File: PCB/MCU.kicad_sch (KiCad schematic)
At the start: 17 parts, among them J2 Conn_01x05_Pin, SW1 SW_Push, U1 STM32WLE5CCUx

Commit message: added power block, pheripherial
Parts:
- SW1: value SW_Push -> SKRKAHE020
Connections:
- net UART_RX renamed UART0_RX
- net UART_TX renamed UART0_TX
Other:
- added sheet Pheripherials (pheripherials.kicad_sch)
- moved on the sheet: C1, J2, R1, R2, R3, SW1

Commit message: added GPS, charging IC, SHT41, and started working on the RF
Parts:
- added C16: 100nF, 1_capacitor_SMD:C_0402_1005Metric, symbol 0_generic_component:C
- added C17: 47pF, 1_capacitor_SMD:C_0402_1005Metric, symbol 0_generic_component:C
- added C18: 1,2pF, 1_capacitor_SMD:C_0402_1005Metric, symbol 0_generic_component:C
- added C19: 220nF, 1_capacitor_SMD:C_0402_1005Metric, symbol 0_generic_component:C
- added C20: 10pF, 1_capacitor_SMD:C_0402_1005Metric, symbol 0_generic_component:C
- added FB1: 1400Ω/1GHz, 2_inductor_SMD:L_0402_1005Metric, symbol 0_generic_component:ferrite_bead
- added J3: Conn_01x02_Pin, 300_pin_header_connector:PinHeader_1x02_P2.54mm_Vertical, symbol 0_generic_component:Conn_01x02_Pin
- added R12: 220Ω, 0_resistor_SMD:R_0402_1005Metric, symbol 0_generic_component:R
- added R13: 10KΩ, 0_resistor_SMD:R_0402_1005Metric, symbol 0_generic_component:R
- added Y1: ECS-TXO-25CSMV, 20_oscillator:ECS-TXO-25CSMV, symbol 20_oscillator:ECS-TXO-25CSMV
- U1: Current ~3.5mA in RUN, 120mA 868 Tx -> ~5mA in RX, 120mA 868 Tx
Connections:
- net GND: no longer C1.2, C10.2, C11.2, C12.2, C13.2, C2.2, C6.2, C7.2, C8.2, C9.2, R2.2, SW1.1, U1.48 (VSSSMPS), U1.49 (VSS)
- net UART1_RX: now also U1.10 (PA3)
- net UART1_TX: now also U1.9 (PA2)
- net PH3-BOOT0: now reaches U1.19 (PH3)
- net PH3-BOOT0: now also J3.2 (Pin_2), R13.1
- net RFI_P: now reaches U1.20 (RFI_P)
- net RFI_N: now reaches U1.21 (RFI_N)
- net RFO_HP: now reaches U1.23 (RFO_HP)
- net VR_PA: now reaches U1.24 (VR_PA)
- net OSC_IN: now reaches U1.26 (OSC_IN)
- net OSC_IN: now also C20.2
- net PB0_VDD_TCXO: now reaches U1.30 (PB0)
- net PB0_VDD_TCXO: now also C16.1, C17.1, C18.1, FB1.1
- new net: C20.1, R12.2
- new net: C19.2, FB1.2, Y1.4 (VDD)
- new net: R12.1, Y1.3 (OUTPUT)
- new net +3.3V: J3.1 (Pin_1)
- new net GNDREF: C1.2, C10.2, C11.2, C12.2, C13.2, C16.2, C17.2, C18.2, C19.1, C2.2, C6.2, C7.2, C8.2, C9.2, R13.2, R2.2, SW1.1, U1.48 (VSSSMPS), U1.49 (VSS), Y1.1 (GND), Y1.2 (GND)
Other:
- added sheet RF Frontend (RFfrontend.kicad_sch)
- note added: "Pin defines are based on the wio E5 and rak3172 MT definition."
- moved on the sheet: C1, J2, R1, R2, R3, SW1

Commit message: ported the main mcu from the inpiration board
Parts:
- added C21, C22, C23, C25: 33pF, 1_capacitor_SMD:C_0402_1005Metric, symbol 0_generic_component:C
- added C24, C26: 4,7uF, 1_capacitor_SMD:C_1206_3216Metric, symbol 0_generic_component:C
- added C27, C29, C30, C33: 100nF, 1_capacitor_SMD:C_0402_1005Metric, symbol 0_generic_component:C
- added C28: 470nF, 1_capacitor_SMD:C_0603_1608Metric, symbol 0_generic_component:C
- added C31: 10nF, 1_capacitor_SMD:C_0402_1005Metric, symbol 0_generic_component:C
- added C32: 1uF, 1_capacitor_SMD:C_0603_1608Metric, symbol 0_generic_component:C
- added C34: 47pF, 1_capacitor_SMD:C_0402_1005Metric, symbol 0_generic_component:C
- added C35: 1,2pF, 1_capacitor_SMD:C_0402_1005Metric, symbol 0_generic_component:C
- added D4: User LED Red, 3_LED_SMD:LED_0402_1005Metric, symbol 0_generic_component:LED
- added L3: 15uH, 2_inductor_SMD:L_0805_2012Metric, symbol 0_generic_component:L
- added R14: 340Ω, 0_resistor_SMD:R_0402_1005Metric, symbol 0_generic_component:R
- added U7: STM32WLE5C8Ux, 100_QFN_package:QFN-48-1EP_7x7mm_P0.5mm_EP5.6x5.6mm_ThermalVias, symbol 100_MCU_ST_STM32WL:STM32WLE5C8Ux
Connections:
- net +3.3V: now also C21.2, C22.2, C23.2, C24.1, C26.1, C27.1, C29.1, C30.1, C31.1, C32.1, R14.2, U7.11 (VDD), U7.25 (VDDPA), U7.28 (VDDRF), U7.37 (VBAT), U7.41 (VDDA), U7.44 (VDD), U7.46 (VDDSMPS)
- net GNDREF: now also C21.1, C22.1, C23.1, C24.2, C25.1, C26.2, C27.2, C28.2, C29.2, C30.2, C31.2, C32.2, C33.2, C34.2, C35.2, U7.48 (VSSSMPS), U7.49 (VSS)
- net NRST: now also U7.18 (NRST)
- net OSC_IN: now also U7.26 (OSC_IN)
- net PB0_VDD_TCXO: now also C33.1, C34.1, C35.1, U7.30 (PB0)
- net PH3-BOOT0: now also U7.19 (PH3)
- net RFI_N: now also U7.21 (RFI_N)
- net RFI_P: now also U7.20 (RFI_P)
- net RFO_HP: now also U7.23 (RFO_HP)
- net SWCLK: now also U7.42 (PA14)
- net SWDIO: now also U7.36 (PA13)
- net VR_PA: now also U7.24 (VR_PA)
- new net: C25.2, C28.1, L3.1, U7.29 (VDDRF1V55), U7.45 (VFBSMPS)
- new net: D4.2 (A), R14.1
- new net: L3.2, U7.47 (VLXSMPS)
- new net: D4.1 (K), U7.15 (PA7)
- new net RF_SWITCH_CTRL: U7.12 (PA4)
- new net SWO: U7.1 (PB3)
- new net USART2_rx: U7.10 (PA3)
- new net USART2_tx: U7.9 (PA2)
- no-connect marks 0 -> 22
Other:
- moved on the sheet: C10, C11, C12, C13, C16, C17, C18, C2, C6, C7, C8, C9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

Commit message: finished the migration
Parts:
- removed U7: STM32WLE5C8Ux, 100_QFN_package:QFN-48-1EP_7x7mm_P0.5mm_EP5.6x5.6mm_ThermalVias, symbol 100_MCU_ST_STM32WL:STM32WLE5C8Ux
- added U7: STM32WLE5CCUx, Package_DFN_QFN:QFN-48-1EP_7x7mm_P0.5mm_EP5.6x5.6mm, symbol MCU_ST_STM32WL:STM32WLE5CCUx
- D4: value User LED Red -> User LED Cyan; PartNumber B1811URO-20D000113U1930 -> (none)
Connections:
- net +3.3V: now also U7.11 (VDD), U7.25 (VDDPA), U7.28 (VDDRF), U7.37 (VBAT), U7.41 (VDDA), U7.44 (VDD), U7.46 (VDDSMPS)
- net GNDREF: now also U7.48 (VSSSMPS), U7.49 (VSS)
- net LED: now also D4.1 (K), U7.15 (PA7), U7.3 (PB5)
- net NRST: now also U7.18 (NRST)
- net OSC_IN: now also U7.26 (OSC_IN)
- net PB0_VDD_TCXO: now also U7.30 (PB0)
- net PH3-BOOT0: now also U7.19 (PH3)
- net RFI_N: now also U7.21 (RFI_N)
- net RFI_P: now also U7.20 (RFI_P)
- net RFO_HP: now also U7.23 (RFO_HP)
- net SCL: now also U7.35 (PA12)
- net SDA: now also U7.34 (PA11)
- net SWCLK: now also U7.42 (PA14)
- net SWDIO: now also U7.36 (PA13)
- net UART0_RX: now also U7.5 (PB7)
- net UART0_TX: now also U7.4 (PB6)
- net UART1_RX: now also U7.10 (PA3)
- net UART1_TX: now also U7.9 (PA2)
- net VR_PA: now also U7.24 (VR_PA)
- net at C25.2, C28.1, L3.1: now also U7.29 (VDDRF1V55), U7.45 (VFBSMPS)
- net at L3.2: now also U7.47 (VLXSMPS)
- no-connect marks 22 -> 18
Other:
- moved on the sheet: C33, C34, C35, D4, R14

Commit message: what about actually comiting
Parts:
- removed C10, C12: 0603 1uF, symbol Device:C
- removed C11, C6, C7: 0603 100nF, symbol Device:C
- removed C13, C8: 0603 4.7uF, symbol Device:C
- removed C16: 100nF, 1_capacitor_SMD:C_0402_1005Metric, symbol 0_generic_component:C
- removed C17: 47pF, 1_capacitor_SMD:C_0402_1005Metric, symbol 0_generic_component:C
- removed C18: 1,2pF, 1_capacitor_SMD:C_0402_1005Metric, symbol 0_generic_component:C
- removed C2: 0603 470nF, symbol Device:C
- removed C9: 0603 10nF, symbol Device:C
- removed D4: User LED Cyan, 3_LED_SMD:LED_0402_1005Metric, symbol 0_generic_component:LED
- removed L2: 15uH, symbol Device:L
- removed R1, R2: 0603 R, symbol Device:R
- removed R14: 340Ω, 0_resistor_SMD:R_0402_1005Metric, symbol 0_generic_component:R
- removed U1: STM32WLE5CCUx, Package_DFN_QFN:QFN-48-1EP_7x7mm_P0.5mm_EP5.6x5.6mm, symbol MCU_ST_STM32WL:STM32WLE5CCUx
- C1: value 0603 100nF -> 100nF; footprint Capacitor_SMD:C_0805_2012Metric_Pad1.18x1.45mm_HandSolder -> Resistor_SMD:R_0603_1608Metric_Pad0.98x0.95mm_HandSolder
- R3: value 0603 10K -> 10K; footprint Resistor_SMD:R_0805_2012Metric_Pad1.20x1.40mm_HandSolder -> Resistor_SMD:R_0603_1608Metric_Pad0.98x0.95mm_HandSolder
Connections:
- net +3V3 is gone; now on net +3.3V: R3.1
- net RF-switch_TX: now reaches U7.38 (PC13)
- net RF-switch_RX: now reaches U7.6 (PB8)
- no-connect marks 18 -> 16
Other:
- moved on the sheet: C1, C19, C20, C21, C22, C23, C24, C25, C26, C27, C28, C29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

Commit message: added the rak4630 module
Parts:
- removed C19: 220nF, 1_capacitor_SMD:C_0402_1005Metric, symbol 0_generic_component:C
- removed C20: 10pF, 1_capacitor_SMD:C_0402_1005Metric, symbol 0_generic_component:C
- removed C21, C22, C23, C25: 33pF, 1_capacitor_SMD:C_0402_1005Metric, symbol 0_generic_component:C
- removed C24, C26: 4,7uF, 1_capacitor_SMD:C_1206_3216Metric, symbol 0_generic_component:C
- removed C27, C29, C30, C33: 100nF, 1_capacitor_SMD:C_0402_1005Metric, symbol 0_generic_component:C
- removed C28: 470nF, 1_capacitor_SMD:C_0603_1608Metric, symbol 0_generic_component:C
- removed C31: 10nF, 1_capacitor_SMD:C_0402_1005Metric, symbol 0_generic_component:C
- removed C32: 1uF, 1_capacitor_SMD:C_0603_1608Metric, symbol 0_generic_component:C
- removed C34: 47pF, 1_capacitor_SMD:C_0402_1005Metric, symbol 0_generic_component:C
- removed C35: 1,2pF, 1_capacitor_SMD:C_0402_1005Metric, symbol 0_generic_component:C
- removed FB1: 1400Ω/1GHz, 2_inductor_SMD:L_0402_1005Metric, symbol 0_generic_component:ferrite_bead
- removed J3: Conn_01x02_Pin, 300_pin_header_connector:PinHeader_1x02_P2.54mm_Vertical, symbol 0_generic_component:Conn_01x02_Pin
- removed L3: 15uH, 2_inductor_SMD:L_0805_2012Metric, symbol 0_generic_component:L
- removed R12: 220Ω, 0_resistor_SMD:R_0402_1005Metric, symbol 0_generic_component:R
- removed R13: 10KΩ, 0_resistor_SMD:R_0402_1005Metric, symbol 0_generic_component:R
- removed U7: STM32WLE5CCUx, Package_DFN_QFN:QFN-48-1EP_7x7mm_P0.5mm_EP5.6x5.6mm, symbol MCU_ST_STM32WL:STM32WLE5CCUx
- removed Y1: ECS-TXO-25CSMV, 20_oscillator:ECS-TXO-25CSMV, symbol 20_oscillator:ECS-TXO-25CSMV
- added J1: UJ20-C-H-G-SMT-2A-P16-TR, Connector_USB:USB_C_Receptacle_HRO_TYPE-C-31-M-12, symbol Connector:USB_C_Receptacle_USB2.0_16P
- added R4, R5: 0603 5k1, Resistor_SMD:R_0805_2012Metric_Pad1.20x1.40mm_HandSolder, symbol Device:R
- added U1: RAK4630, RAK4630:RAK4630, symbol RAK4630:RAK4630
- added U2: USBLC6-2SC6, Package_TO_SOT_SMD:SOT-23-6, symbol Power_Protection:USBLC6-2SC6
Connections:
- net NRST is gone; now on net RST: J2.5 (Pin_5)
- net GNDREF: now also J1.A1 (GND), J1.A12 (GND), J1.B1 (GND), J1.B12 (GND), J1.SH (SHIELD), R4.2, R5.2, U1.14 (GND1), U1.16 (GND2), U1.22 (GND3), U1.35 (GND4), U1.36 (GND5), U1.38 (GND6), U1.42 (GND7), U2.2 (GND)
- new net +3V3: U1.20 (VBAT_SX), U1.21 (VBAT_IO_SX), U1.43 (VDD_NRF), U1.44 (VBAT_NRF)
- new net CC1: J1.A5 (CC1), R4.1
- new net CC2: J1.B5 (CC2), R5.1
- new net D+: J1.A6 (D+), J1.B6 (D+), U2.3 (I/O2)
- new net D-: J1.A7 (D-), J1.B7 (D-), U2.1 (I/O1)
- new net USB_D+: U1.3 (USB+), U2.4 (I/O2)
- new net USB_D-: U1.2 (USB-), U2.6 (I/O1)
- new net VBUS: J1.A4 (VBUS), J1.A9 (VBUS), J1.B4 (VBUS), J1.B9 (VBUS), U1.1 (VBUS), U2.5 (VBUS)
- no-connect marks 16 -> 2
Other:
- removed sheet RF Frontend
- removed sheet USBC_UART
- sheet Pheripherials ports: added LED; removed none
- note added: "500mA - 3A @ 5V"
- note removed: "Pin defines are based on the wio E5 and rak3172 MT definition."
- moved on the sheet: C1, R3, SW1

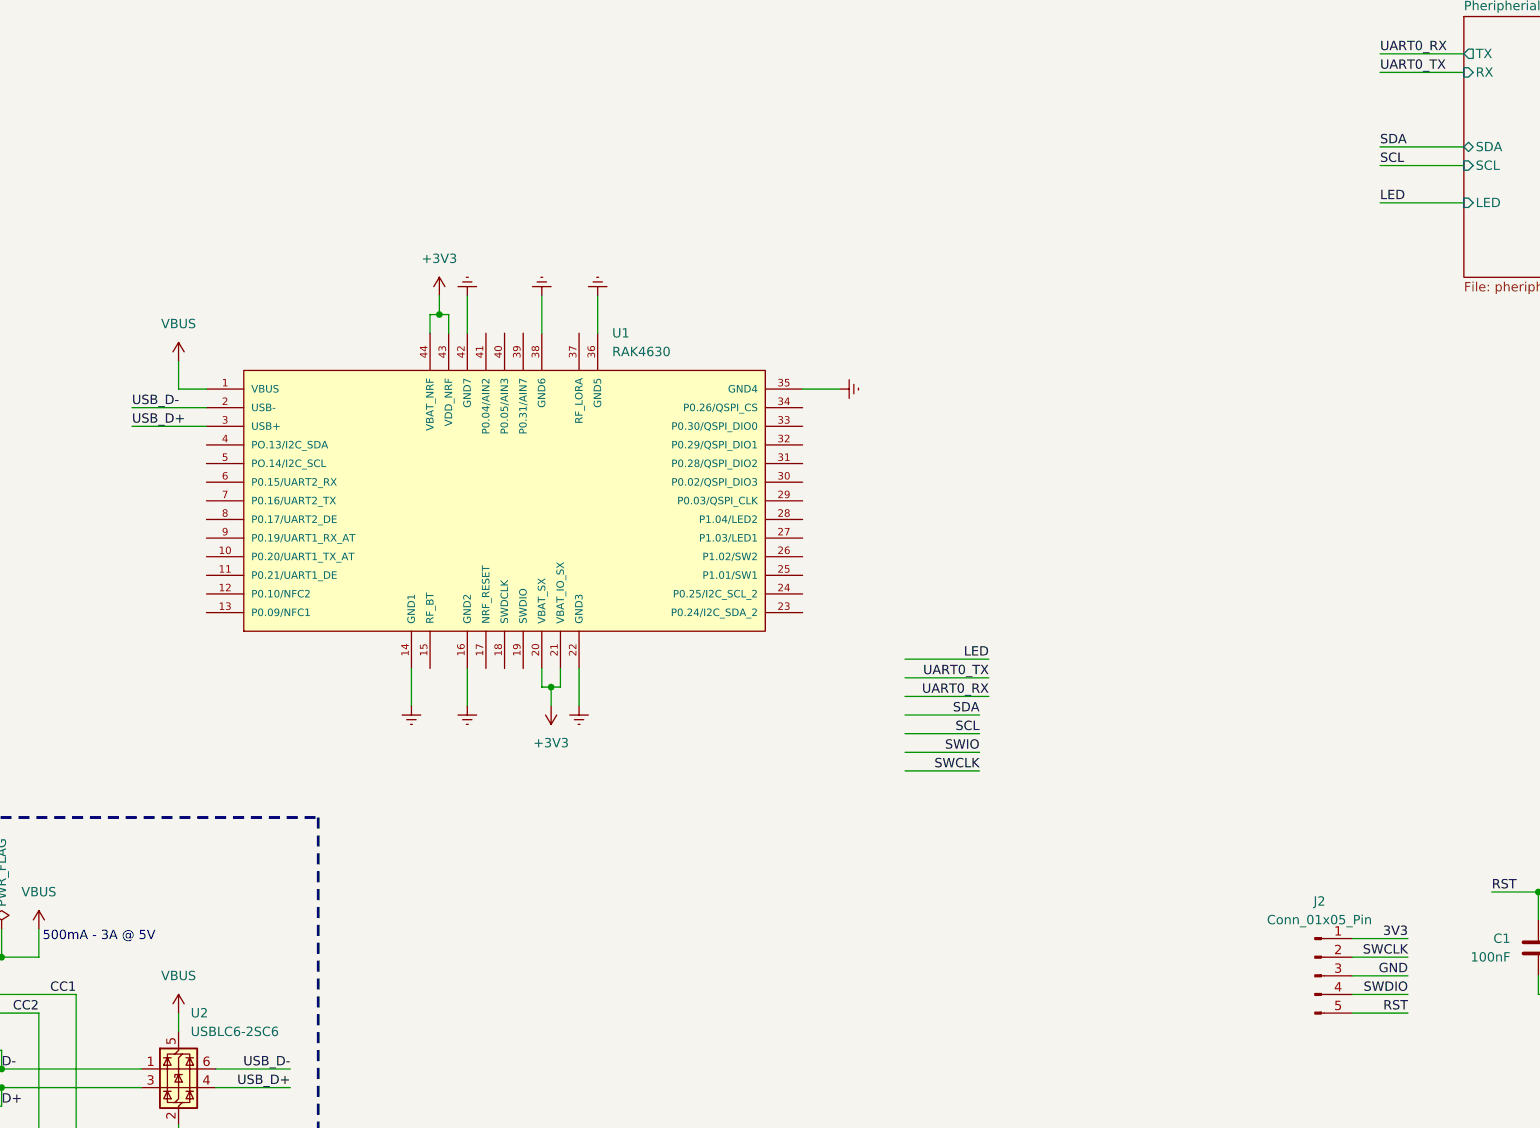
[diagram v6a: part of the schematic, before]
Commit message: marked pin functions and started working on the pheripherials
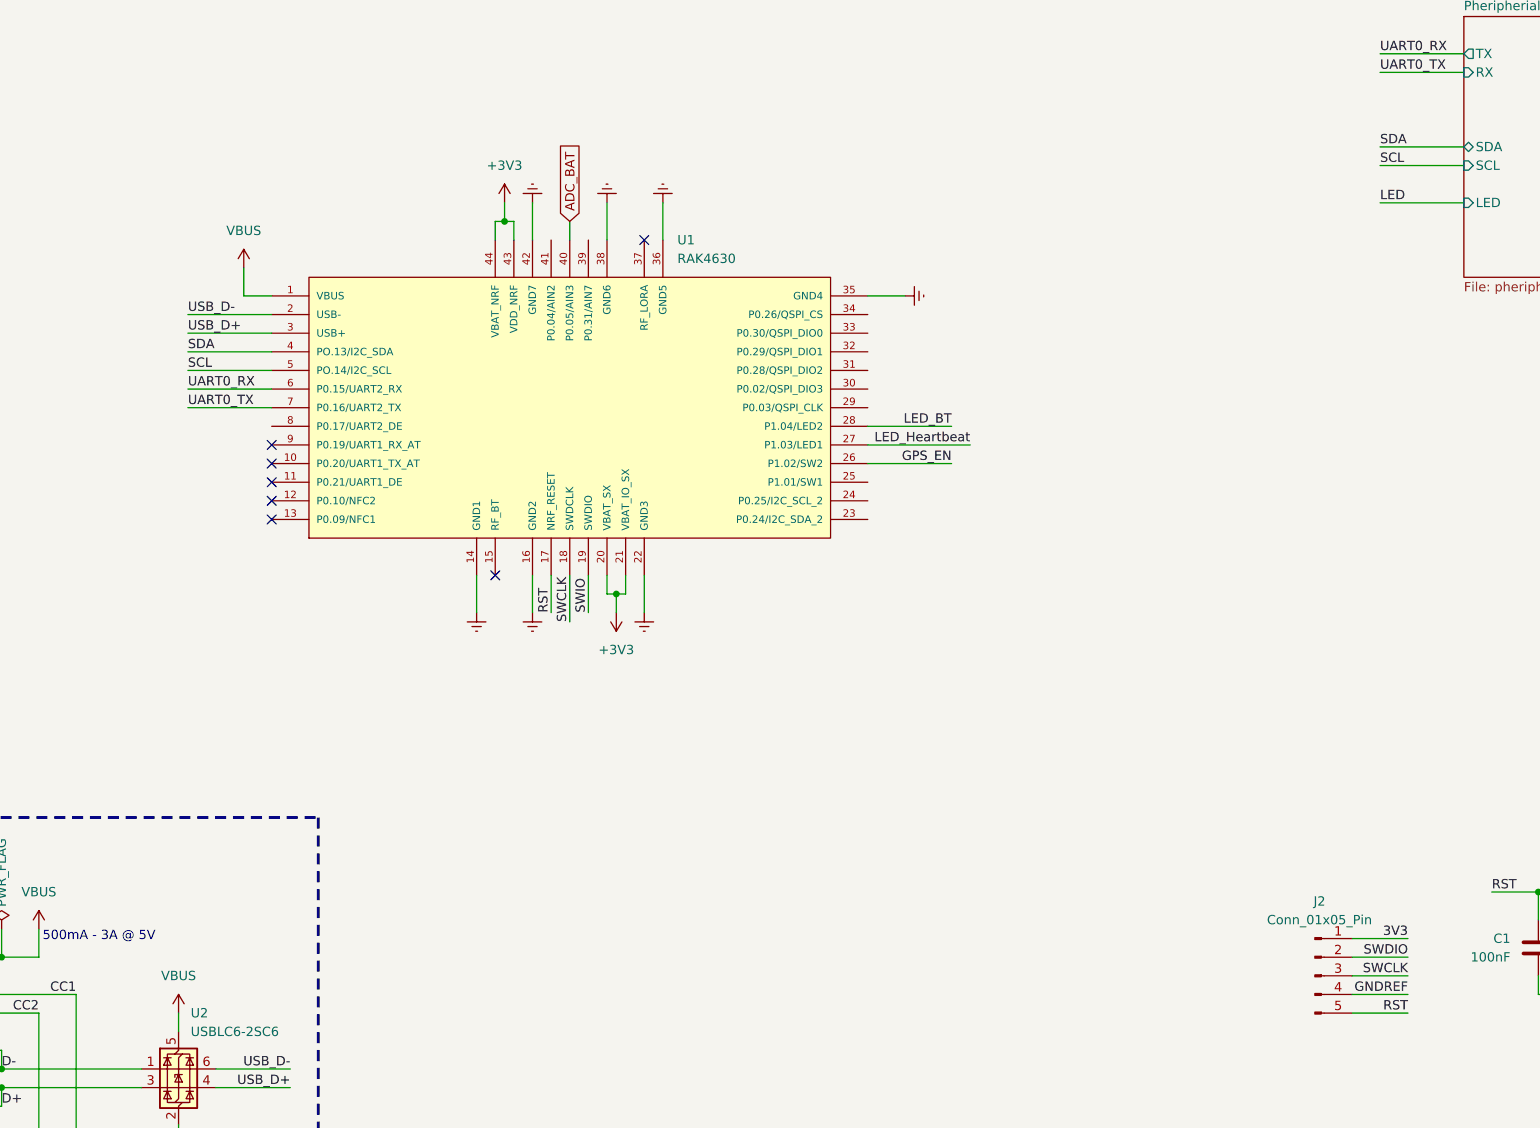
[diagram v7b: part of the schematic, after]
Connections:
- net GND is gone; now on net SWCLK: J2.3 (Pin_3)
- net GNDREF: now also J2.4 (Pin_4)
- net RST: now also U1.17 (NRF_RESET)
- net SCL: now also U1.5 (PO.14/I2C_SCL)
- net SDA: now also U1.4 (PO.13/I2C_SDA)
- net SWCLK: now also U1.18 (SWDCLK); no longer J2.2 (Pin_2)
- net SWDIO: now also J2.2 (Pin_2); no longer J2.4 (Pin_4)
- net SWIO: now also U1.19 (SWDIO)
- net UART0_RX: now also U1.6 (P0.15/UART2_RX)
- net UART0_TX: now also U1.7 (P0.16/UART2_TX)
- net GPS_EN: now reaches U1.26 (P1.02/SW2)
- net LED_Heartbeat: now reaches U1.27 (P1.03/LED1)
- net LED_BT: now reaches U1.28 (P1.04/LED2)
- net ADC_BAT: now reaches U1.40 (P0.05/AIN3)
- no-connect marks 2 -> 9
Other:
- moved on the sheet: U1
